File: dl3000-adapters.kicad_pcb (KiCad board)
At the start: 2 copper layers, 57 x 68 mm, 11 parts, among them J1 Banana Jack, J2 BNC, J3 Banana Jack, J4 Banana Jack, J5 Banana Jack

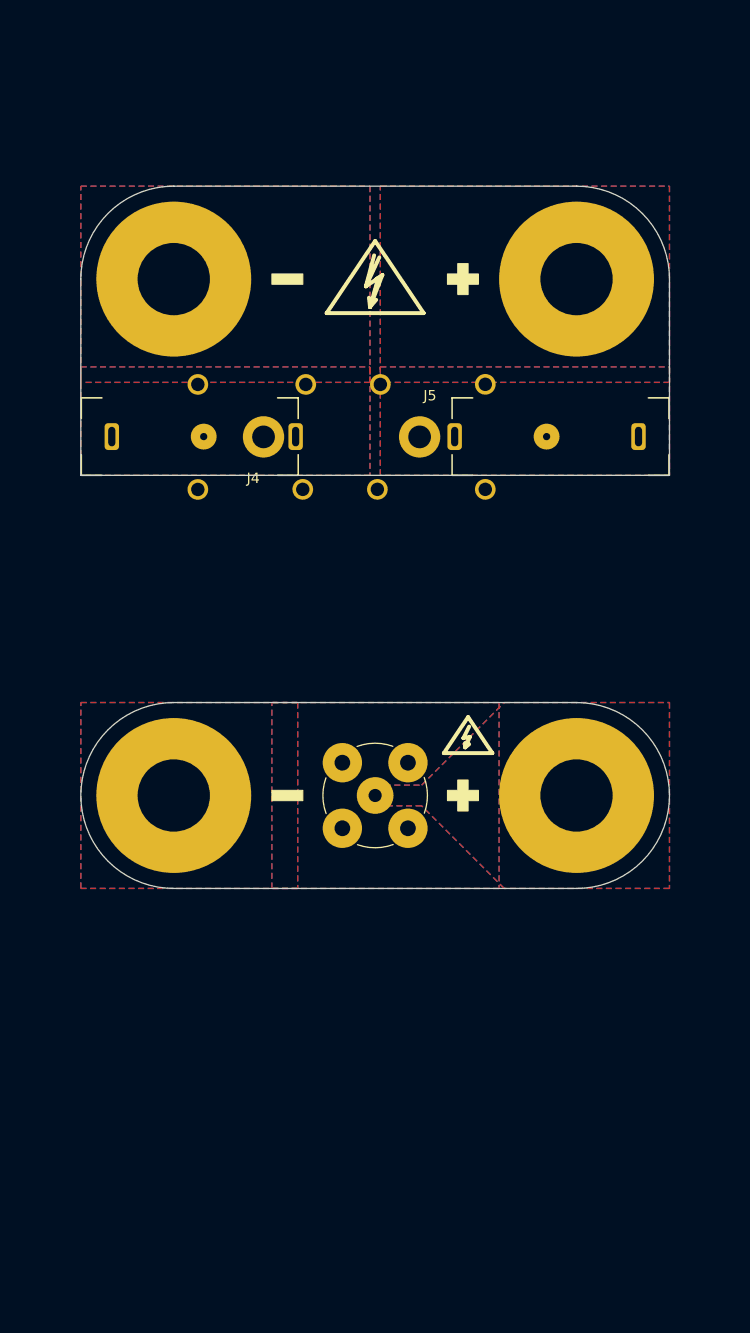
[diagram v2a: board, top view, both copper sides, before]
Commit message: Add separate board for Pomona jacks
It would be too much of a hassle to have both banana jack footprints
overlap on the same board.
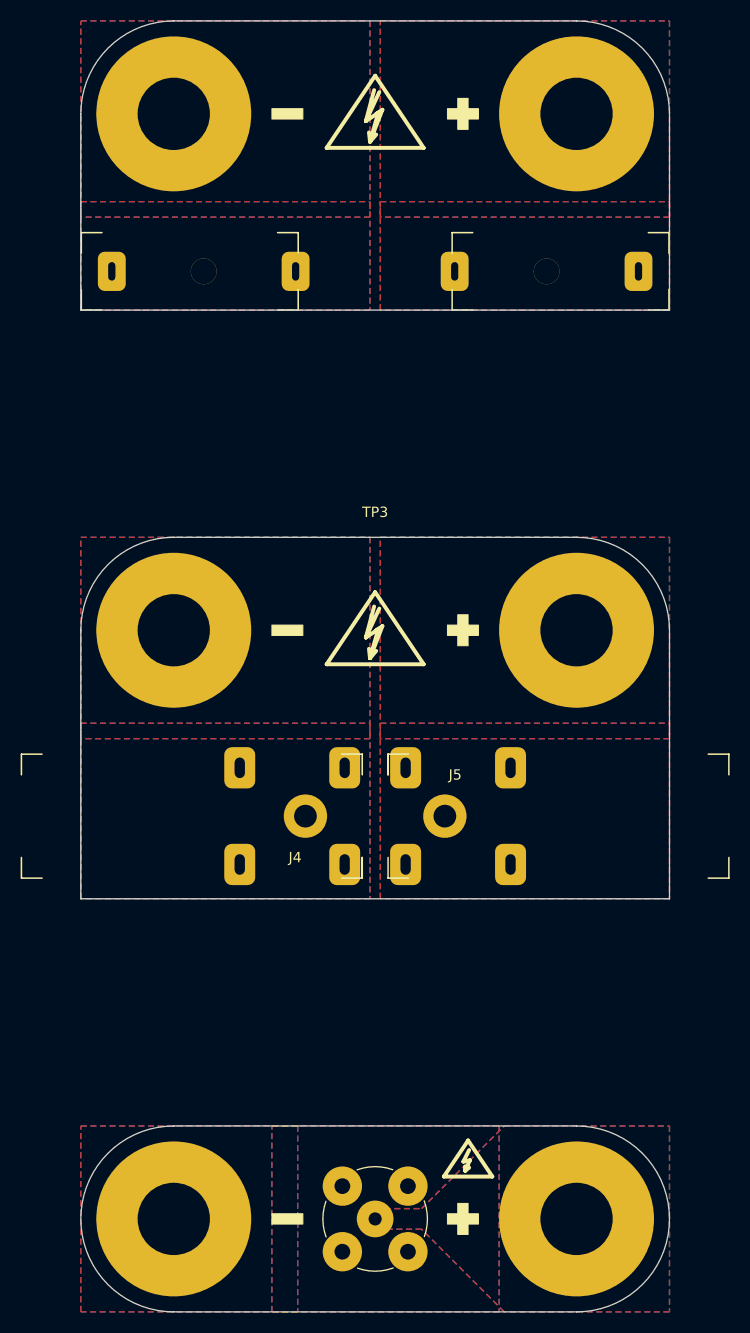
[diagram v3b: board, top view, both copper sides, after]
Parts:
- removed the REF** at (150.0, 50.5)
- removed the REF** at (150.0, 51.5)
- removed the REF** at (141.5, 100.0)
- added REF**: OSHW-Logo_5.7x6mm_SilkScreen, Symbol:OSHW-Logo_5.7x6mm_SilkScreen, B.Cu at (150.0, 86.0)
- added REF**: Symbol_HighVoltage_Type2_SilkScreenTop_VerySmall, Symbol_Local:Symbol_HighVoltage_Type2_SilkScreenTop_VerySmall, F.Cu at (150.0, 84.5)
- added REF**: Symbol_HighVoltage_Type2_SilkScreenTop_VerySmall, Symbol_Local:Symbol_HighVoltage_Type2_SilkScreenTop_VerySmall, F.Cu at (150.0, 34.5)
- added REF**: OSHW-Logo_5.7x6mm_SilkScreen, Symbol:OSHW-Logo_5.7x6mm_SilkScreen, B.Cu at (150.0, 36.0)
- added REF**: OSHW-Logo_5.7x6mm_SilkScreen, Symbol:OSHW-Logo_5.7x6mm_SilkScreen, B.Cu at (141.5, 141.0)
- added TP3: Binding Posts, TestPoint_Local:TestPoint_2Pads_D15.0mm_Drill7.0mm_RIGOL_DL3000_Binding_Posts, F.Cu at (150.0, 84.0)
- moved J2 41.0 mm to (150.0, 141.0)
- moved REF** 41.0 mm to (159.0, 135.5)
- moved TP2 41.0 mm to (150.0, 141.0)
- moved J4 36.9 mm to (143.2, 102.0)
- moved J5 36.8 mm to (156.8, 102.0)
- moved J1 16.0 mm to (124.5, 49.2)
- moved J3 16.0 mm to (175.5, 49.2)
- moved TP1 16.0 mm to (150.0, 34.0)
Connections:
- J1 pad 1: /BANANA- -> /BANANA_PB4-
- J3 pad 1: /BANANA+ -> /BANANA_PB4+
- J4 pad 1: /BANANA- -> /BANANA_73099-
- J5 pad 1: /BANANA+ -> /BANANA_73099+
- TP1 pad 1: /BANANA- -> /BANANA_PB4-
- TP1 pad 2: /BANANA+ -> /BANANA_PB4+
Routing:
- added copper zone on B.Cu, net /BANANA_73099+
- added copper zone on F.Cu, net /BANANA_73099+
- added copper zone on B.Cu, net /BANANA_73099-
- added copper zone on F.Cu, net /BANANA_73099-
- added copper zone on B.Cu, net /BANANA_PB4+
- added copper zone on F.Cu, net /BANANA_PB4+
- added copper zone on B.Cu, net /BANANA_PB4-
- added copper zone on F.Cu, net /BANANA_PB4-
- removed copper zone on B.Cu, net /BANANA+
- removed copper zone on F.Cu, net /BANANA+
- removed copper zone on B.Cu, net /BANANA-
- removed copper zone on F.Cu, net /BANANA-
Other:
- board size 57 x 68 mm -> 57 x 125 mm
- board text added: "1.1"
- board text added: "DL3000 Banana Jack Adapter for Hirschmann SKS PB4"
- board text added: "DL3000 Banana Jack Adapter for Pomona 73099"
- board text removed: "DL3000 Banana Jack Adapter"
